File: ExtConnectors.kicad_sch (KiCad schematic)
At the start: 13 parts, among them J1 USB_C_Receptacle_USB2.0_16P, J2 DBG, J3 Btn_OffBoard, J4 Batt_In, J5 WS2812, U2 TPD2E2U06, U3 AP2112K-3.3, U6 TVS0500DRV

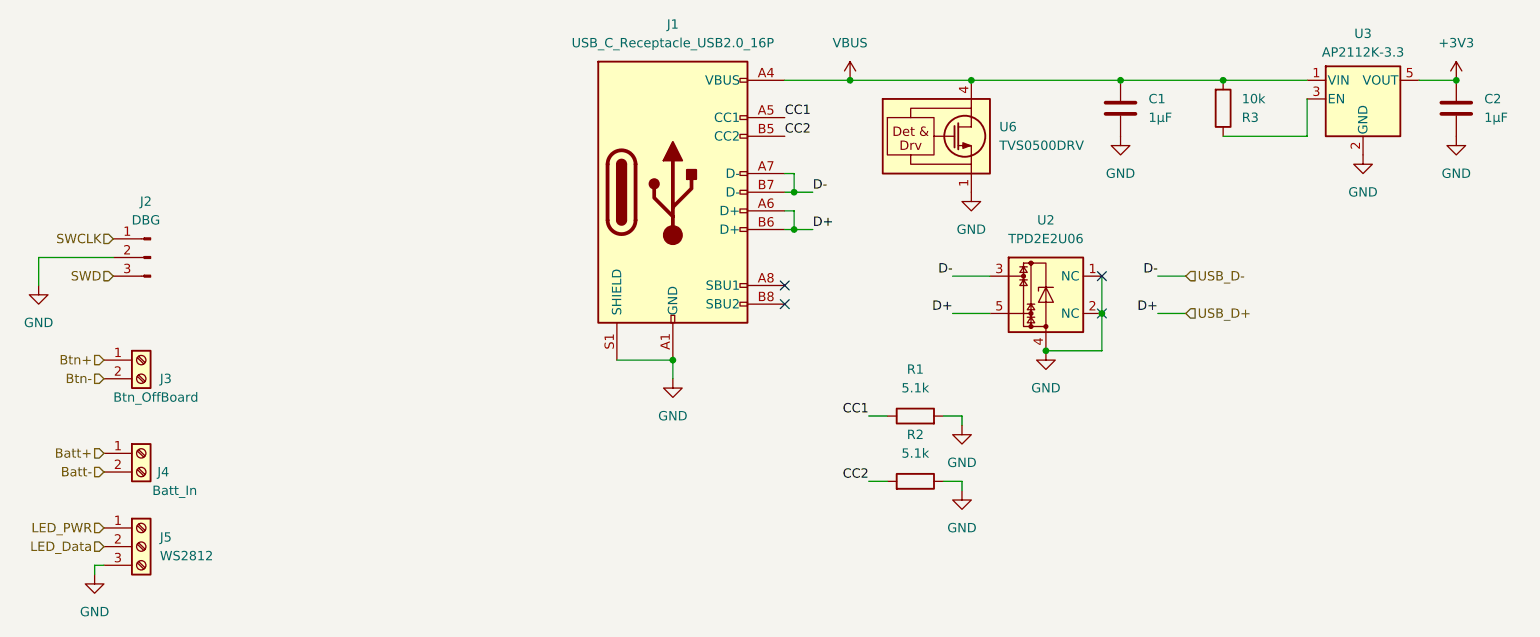
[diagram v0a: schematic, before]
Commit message: WIP: Updated SK6812Mini to SK6812Mini-E and remapped ref des keys between PCB and Schematic.
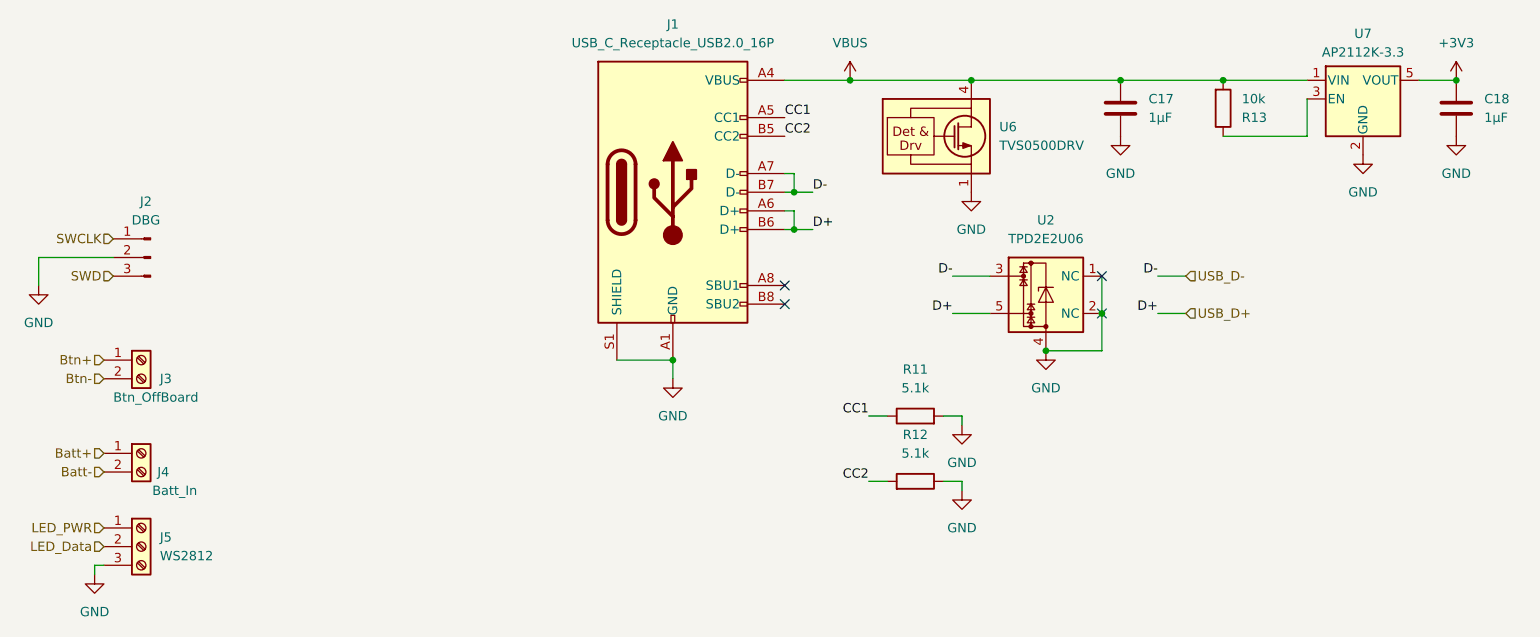
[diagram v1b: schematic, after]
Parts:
- removed C1, C2: 1μF, Capacitor_SMD:C_0603_1608Metric_Pad1.08x0.95mm_HandSolder, symbol Device:C
- removed R1, R2: 5.1k, Resistor_SMD:R_0603_1608Metric_Pad0.98x0.95mm_HandSolder, symbol Device:R
- added C17, C18: 1μF, Capacitor_SMD:C_0603_1608Metric_Pad1.08x0.95mm_HandSolder, symbol Device:C
- added R11, R12: 5.1k, Resistor_SMD:R_0603_1608Metric_Pad0.98x0.95mm_HandSolder, symbol Device:R
- renumbered R3 to R13, U3 to U7
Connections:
- net +3V3: now also C18.1
- net CC1: now also R11.1
- net CC2: now also R12.2
- net GND: now also C17.2, C18.2, R11.2, R12.1
- net VBUS: now also C17.1

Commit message: Placing nearly all components onto the PCB. Removing the 9Vto5V battery input stage from populating onto the PCB.
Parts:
- C17, C18: footprint Capacitor_SMD:C_0603_1608Metric_Pad1.08x0.95mm_HandSolder -> Capacitor_SMD:C_0805_2012Metric_Pad1.18x1.45mm_HandSolder
- R11, R12, R13: footprint Resistor_SMD:R_0603_1608Metric_Pad0.98x0.95mm_HandSolder -> Resistor_SMD:R_0805_2012Metric_Pad1.20x1.40mm_HandSolder
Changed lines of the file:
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@@
 			)
 		)
-		(property "Footprint" "Resistor_SMD:R_0603_1608Metric_Pad0.98x0.95mm_HandSolder"
+		(property "Footprint" "Resistor_SMD:R_0805_2012Metric_Pad1.20x1.40mm_HandSolder"
 			(at 190.5 95.758 90)
 			(effects
@@
 			)
 		)
-		(property "Footprint" "Capacitor_SMD:C_0603_1608Metric_Pad1.08x0.95mm_HandSolder"
+		(property "Footprint" "Capacitor_SMD:C_0805_2012Metric_Pad1.18x1.45mm_HandSolder"
 			(at 219.4052 55.88 0)
 			(effects
@@
 			)
 		)
-		(property "Footprint" "Resistor_SMD:R_0603_1608Metric_Pad0.98x0.95mm_HandSolder"
+		(property "Footprint" "Resistor_SMD:R_0805_2012Metric_Pad1.20x1.40mm_HandSolder"
 			(at 190.5 104.648 90)
 			(effects
@@
 			)
 		)
-		(property "Footprint" "Resistor_SMD:R_0603_1608Metric_Pad0.98x0.95mm_HandSolder"
+		(property "Footprint" "Resistor_SMD:R_0805_2012Metric_Pad1.20x1.40mm_HandSolder"
 			(at 230.632 52.07 90)
 			(effects
@@
 		(exclude_from_sim no)
 		(in_bom yes)
-		(on_board yes)
+		(on_board no)
 		(dnp no)
 		(property "Reference" "J3"
@@
 			)
 		)
-		(property "Footprint" "Capacitor_SMD:C_0603_1608Metric_Pad1.08x0.95mm_HandSolder"
+		(property "Footprint" "Capacitor_SMD:C_0805_2012Metric_Pad1.18x1.45mm_HandSolder"
 			(at 265.1252 55.88 0)
 			(effects
@@
 		(exclude_from_sim no)
 		(in_bom yes)
-		(on_board yes)
+		(on_board no)
 		(dnp no)
 		(property "Reference" "J4"

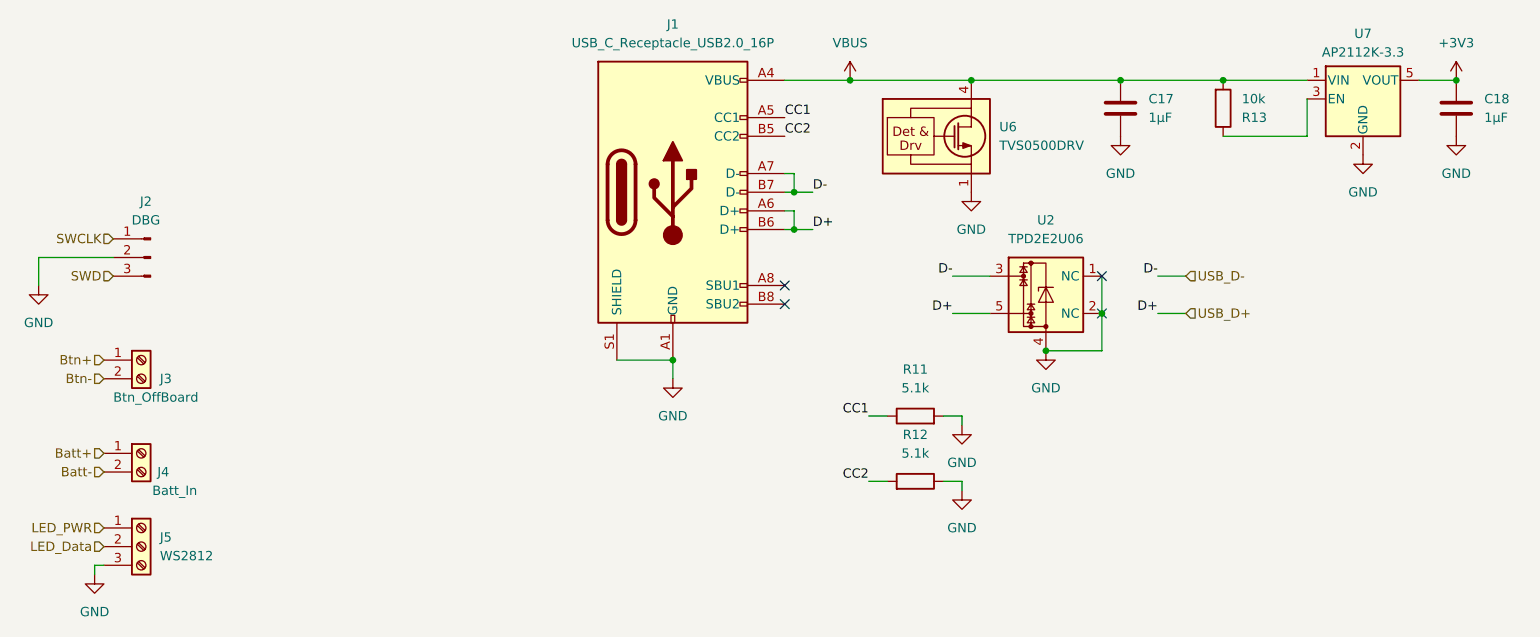
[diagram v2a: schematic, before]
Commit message: Added testpoints, finished placing components, fixed footprint mapping, and ready to start routing tracks.
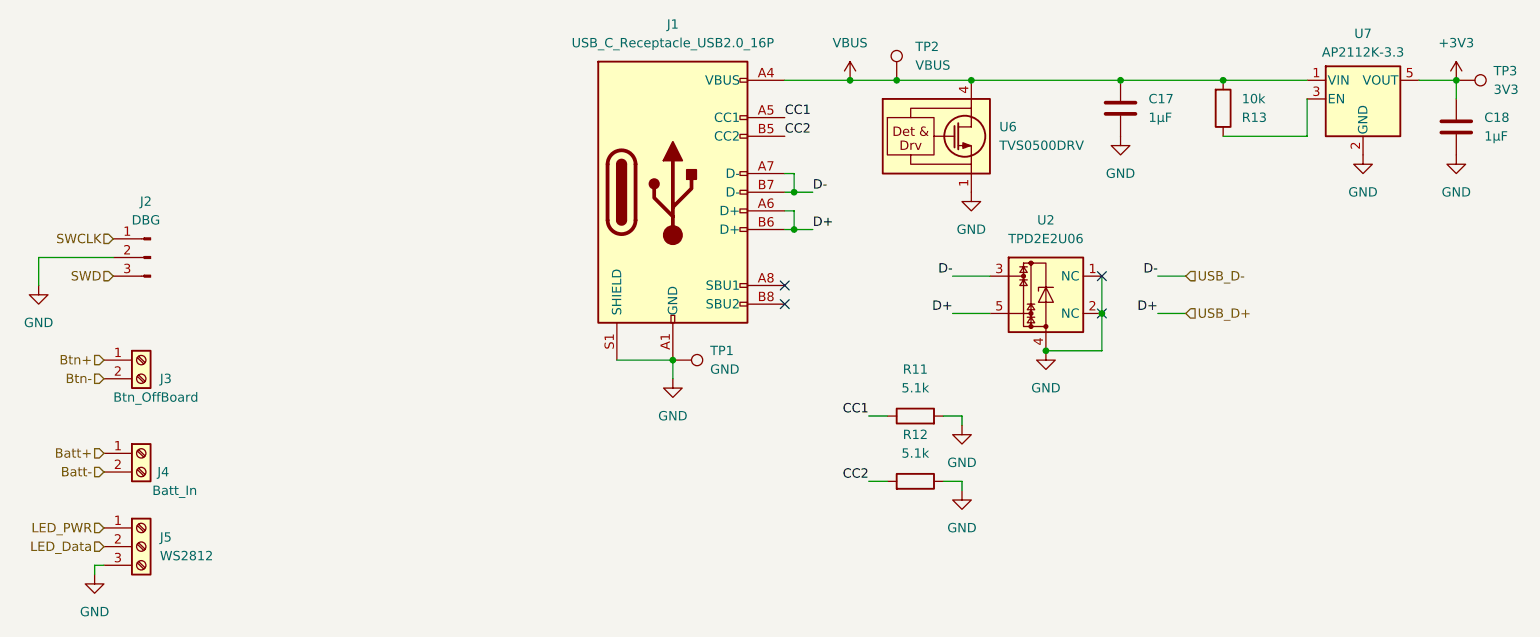
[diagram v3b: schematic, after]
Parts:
- added TP1: GND, TestPoint:TestPoint_Pad_1.5x1.5mm, symbol Connector:TestPoint
- added TP2: VBUS, TestPoint:TestPoint_Pad_D1.5mm, symbol Connector:TestPoint
- added TP3: 3V3, TestPoint:TestPoint_Pad_D1.5mm, symbol Connector:TestPoint
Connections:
- net +3V3: now also TP3.1
- net GND: now also TP1.1
- net VBUS: now also TP2.1
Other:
- moved on the sheet: C18

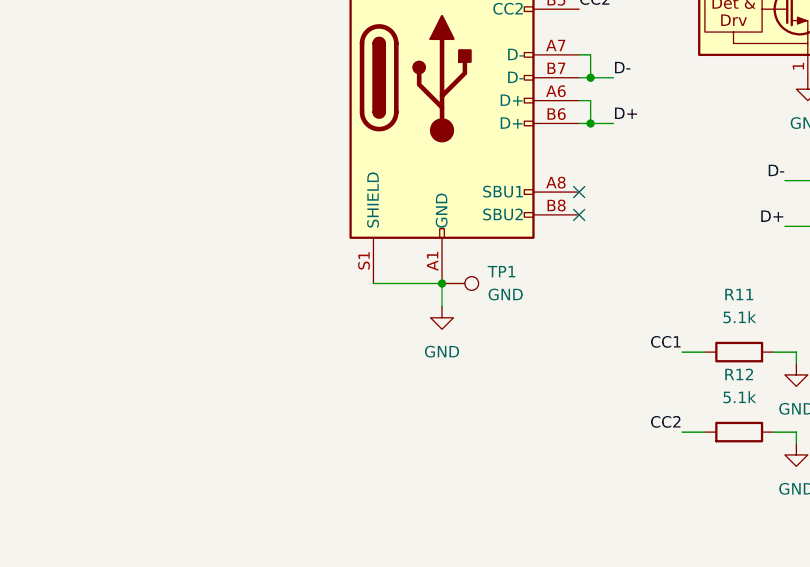
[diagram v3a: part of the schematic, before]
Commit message: Adding additional LEDs and driver to test per-key LEDs, updating net classes and design constraints, and starting to route tracks.
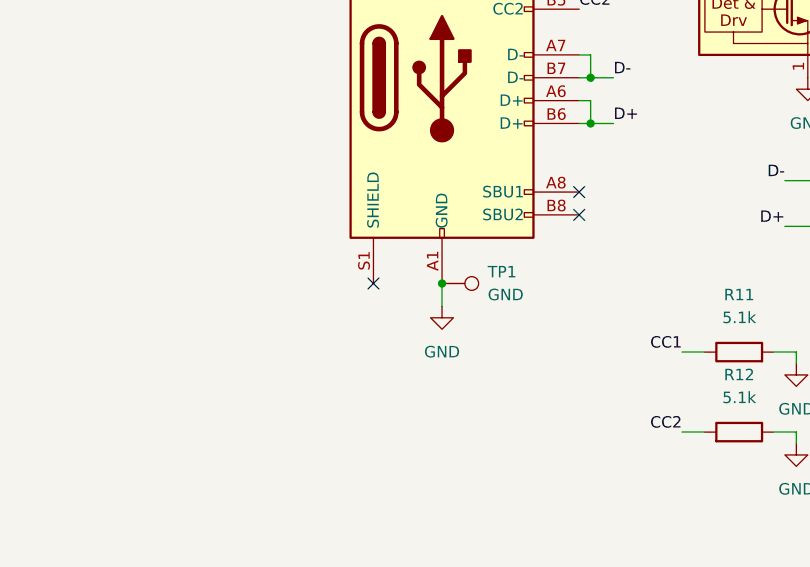
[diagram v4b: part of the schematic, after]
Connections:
- net GND: no longer J1.S1 (SHIELD)
- no-connect marks 4 -> 5
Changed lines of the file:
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@@
+	)
+	(no_connect
+		(at 149.86 86.36)
 	)
 	(no_connect
@@
 		)
 		(stroke
-			(width 0)
-			(type default)
-		)
-	)
-	(wire
-		(pts
-			(xy 149.86 86.36) (xy 157.48 86.36)
-		)
-		(stroke
